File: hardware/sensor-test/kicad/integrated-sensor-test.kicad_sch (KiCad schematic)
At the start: 79 parts, among them J1 TYPE-C-31-M-12, J2 Conn_01x02, J3 USB_B_Micro, J4 Conn_02x18_Odd_Even, SW1 Conn_02x18_Odd_Even, U1 NCP1117-3.3_SOT223, U10 USBLC6-2SC6, U103 RP2040, U2 W25Q128JVS, U3 AP2112K-3.3TRG1, U4 TPS22919DCKR, U5 TMUX1208PWR, U6 DRV5055A3QDBZR, U7 DRV5055A3QDBZR, U8 DRV5055A3QDBZR, U9 DRV5055A3QDBZR, Y1 ABLS-12.000MHZ-B4-T

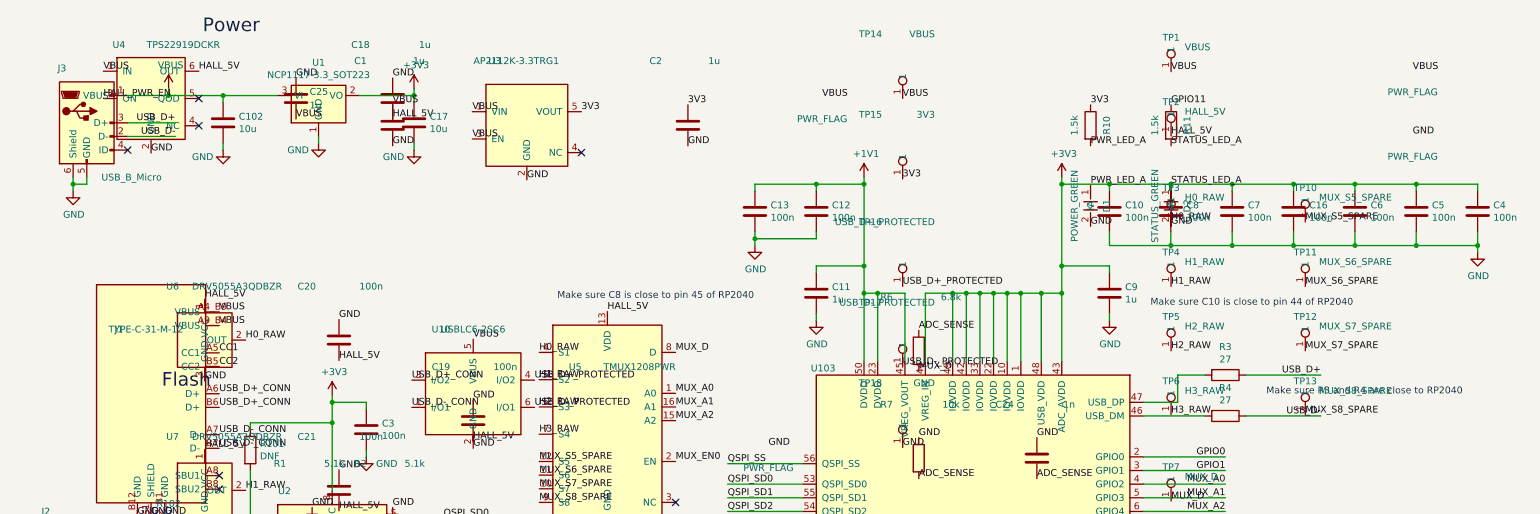
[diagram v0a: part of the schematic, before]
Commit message: Fix integrated schematic power declarations
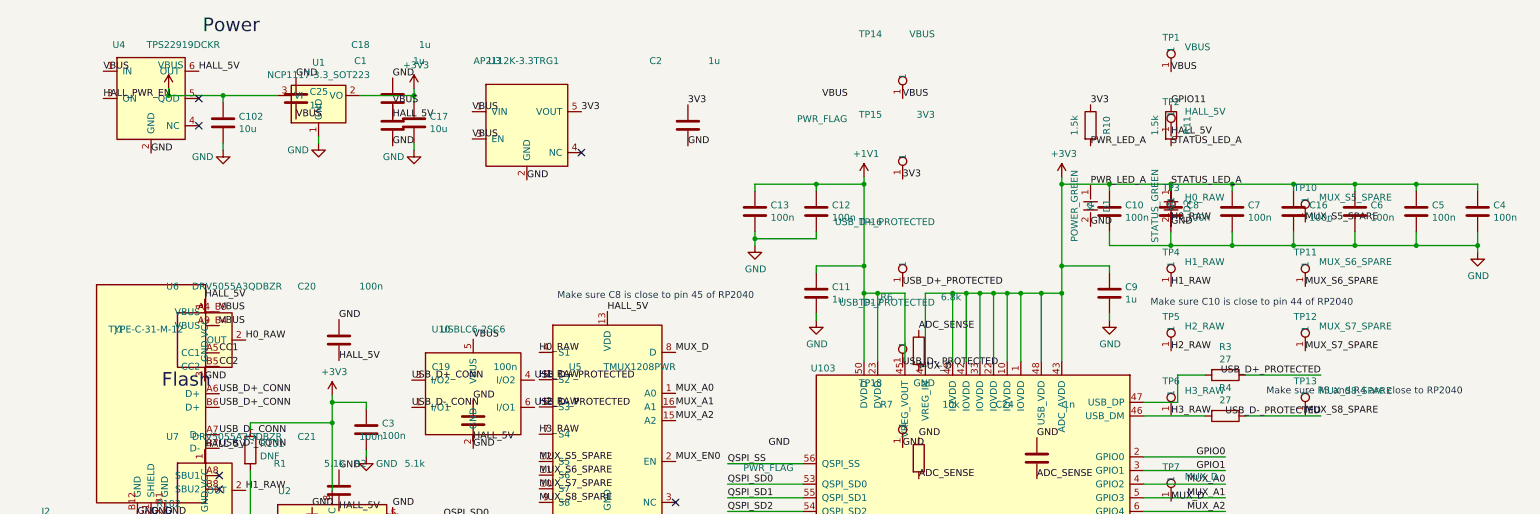
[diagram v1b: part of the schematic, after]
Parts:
- removed J3: USB_B_Micro, RP2040_minimal:USB_Micro-B_Amphenol_10103594-0001LF_Horizontal_modified, symbol RP2040_minimal-rescue:USB_B_Micro-Connector
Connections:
- net USB_D+ is gone; now on net USB_D+_PROTECTED: R3.1
- net USB_D- is gone; now on net USB_D-_PROTECTED: R4.1
- no-connect marks 7 -> 6
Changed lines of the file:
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@@
   (junction (at 312.42 142.24) (diameter 0) (color 0 0 0 0)
     )
-  (junction (at 30.48 60.96) (diameter 0) (color 0 0 0 0)
-    )
   (junction (at 214.63 81.28) (diameter 0) (color 0 0 0 0)
     )
@@
   (junction (at 48.26 44.45) (diameter 0) (color 0 0 0 0)
     )
-  (no_connect (at 40.64 54.61))
   (wire (pts (xy 196.85 93.98) (xy 196.85 81.28))
       (stroke (width 0) (type default))
@@
       (stroke (width 0) (type default))
     )
-  (wire (pts (xy 30.48 60.96) (xy 30.48 62.23))
-      (stroke (width 0) (type default))
-    )
   (wire (pts (xy 236.22 96.52) (xy 236.22 101.6))
       (stroke (width 0) (type default))
@@
       (stroke (width 0) (type default))
     )
-  (wire (pts (xy 30.48 59.69) (xy 30.48 60.96))
-      (stroke (width 0) (type default))
-    )
   (wire (pts (xy 280.67 69.85) (xy 280.67 72.39))
       (stroke (width 0) (type default))
@@
       (stroke (width 0) (type default))
     )
-  (wire (pts (xy 40.64 49.53) (xy 49.53 49.53))
-      (stroke (width 0) (type default))
-    )
   (wire (pts (xy 312.42 124.46) (xy 312.42 127))
       (stroke (width 0) (type default))
@@
       (stroke (width 0) (type default))
     )
-  (wire (pts (xy 33.02 59.69) (xy 33.02 60.96))
-      (stroke (width 0) (type default))
-    )
   (wire (pts (xy 152.4 116.84) (xy 166.37 116.84))
       (stroke (width 0) (type default))
@@
       (stroke (width 0) (type default))
     )
-  (wire (pts (xy 40.64 52.07) (xy 49.53 52.07))
-      (stroke (width 0) (type default))
-    )
   (wire (pts (xy 229.87 104.14) (xy 241.3 104.14))
       (stroke (width 0) (type default))
@@
       (stroke (width 0) (type default))
     )
-  (wire (pts (xy 40.64 44.45) (xy 48.26 44.45))
-      (stroke (width 0) (type default))
-    )
   (wire (pts (xy 339.09 144.78) (xy 326.39 144.78))
       (stroke (width 0) (type default))
@@
       (stroke (width 0) (type default))
     )
-  (wire (pts (xy 33.02 60.96) (xy 30.48 60.96))
-      (stroke (width 0) (type default))
-    )
   (wire (pts (xy 246.38 60.96) (xy 257.81 60.96))
       (stroke (width 0) (type default))
@@
       (effects (font (size 1.27 1.27)) (justify right bottom))
     )
-  (label "USB_D+" (at 262.89 96.52 180) (fields_autoplaced)
+  (label "USB_D+_PROTECTED" (at 262.89 96.52 180) (fields_autoplaced)
       (effects (font (size 1.27 1.27)) (justify right bottom))
     )
@@
       (effects (font (size 1.27 1.27)) (justify right bottom))
     )
-  (label "USB_D+" (at 49.53 49.53 180) (fields_autoplaced)
-      (effects (font (size 1.27 1.27)) (justify right bottom))
-    )
   (label "GPIO1" (at 339.09 127 180) (fields_autoplaced)
       (effects (font (size 1.27 1.27)) (justify right bottom))
@@
       (effects (font (size 1.27 1.27)) (justify right bottom))
     )
-  (label "USB_D-" (at 49.53 52.07 180) (fields_autoplaced)
-      (effects (font (size 1.27 1.27)) (justify right bottom))
-    )
   (label "GPIO20" (at 358.14 144.78 0) (fields_autoplaced)
       (effects (font (size 1.27 1.27)) (justify left bottom))
@@
       (effects (font (size 1.27 1.27)) (justify left bottom))
     )
-  (label "USB_D-" (at 262.89 104.14 180) (fields_autoplaced)
+  (label "USB_D-_PROTECTED" (at 262.89 104.14 180) (fields_autoplaced)
       (effects (font (size 1.27 1.27)) (justify right bottom))
     )
@@
       )
     )
-  (symbol (lib_id "RP2040_minimal-rescue:USB_B_Micro-Connector") (at 33.02 49.53 0) (unit 1)
-      (in_bom yes) (on_board yes) (dnp no)
-      (property "Reference" "J3" (at 29.21 39.37 0)
-        (effects (font (size 1.27 1.27)) (justify right))
-      )
-      (property "Value" "USB_B_Micro" (at 46.99 59.69 0)
-        (effects (font (size 1.27 1.27)) (justify right))
-      )
-      (property "Footprint" "RP2040_minimal:USB_Micro-B_Amphenol_10103594-0001LF_Horizontal_modified" (at 36.83 50.8 0)
-        (effects (font (size 1.27 1.27)) hide)
-      )
-      (property "Datasheet" "https://datasheet.lcsc.com/lcsc/1912111437_Amphenol-ICC-10103594-0001LF_C428495.pdf" (at 36.83 50.8 0)
-        (effects (font (size 1.27 1.27)) hide)
-      )
-      (property "LCSC" "C428495" (at 33.02 49.53 0)
-        (effects (font (size 1.27 1.27)) hide)
-      )
-      (pin "1")
-      (pin "2")
-      (pin "3")
-      (pin "4")
-      (pin "5")
-      (pin "6")
-      (instances
-        (project "he-piantor-sensor-test"
-          (path "/0b572f4d-42c2-4e67-a259-3bf815f1855a"
-            (reference "J3") (unit 1)
-          )
-        )
-      )
-    )
   (symbol (lib_id "power:GND") (at 198.12 198.12 0) (unit 1)
       (in_bom yes) (on_board yes) (dnp no)
@@
       )
     )
-  (symbol (lib_id "power:GND") (at 30.48 62.23 0) (unit 1)
-      (in_bom yes) (on_board yes) (dnp no)
-      (property "Reference" "#PWR01" (at 30.48 68.58 0)
-        (effects (font (size 1.27 1.27)) hide)
-      )
-      (property "Value" "GND" (at 30.607 66.6242 0)
-        (effects (font (size 1.27 1.27)))
-      )
-      (property "Footprint" "" (at 30.48 62.23 0)
-        (effects (font (size 1.27 1.27)) hide)
-      )
-      (property "Datasheet" "" (at 30.48 62.23 0)
-        (effects (font (size 1.27 1.27)) hide)
-      )
-      (pin "1")
-      (instances
-        (project "he-piantor-sensor-test"
-          (path "/0b572f4d-42c2-4e67-a259-3bf815f1855a"
-            (reference "#PWR01") (unit 1)
-          )
-        )
-      )
-    )
   (symbol (lib_id "power:GND") (at 339.09 166.37 0) (mirror y) (unit 1)
       (in_bom yes) (on_board yes) (dnp no)
@@
       (effects (font (size 1.27 1.27)) (justify left bottom))
     )
-  (symbol (lib_id "power:PWR_FLAG") (at 280 40 0) (unit 1)
-      (in_bom yes) (on_board yes) (dnp no)
-      (property "Reference" "#FLG03" (at 280 41.905 0) (effects (font (size 1.27 1.27)) hide))
-      (property "Value" "PWR_FLAG" (at 280 43.81 0) (effects (font (size 1.27 1.27))))
-      (property "Footprint" "" (at 280 40 0) (effects (font (size 1.27 1.27)) hide))
-      (property "Datasheet" "~" (at 280 40 0) (effects (font (size 1.27 1.27)) hide))
-      (pin "1")
-      (instances (project "hall-front-end" (path "/a1000000-0000-0000-0000-000000000001" (reference "#FLG03") (unit 1))))
-    )
-  (label "VBUS" (at 280 40 0) (effects (font (size 1.27 1.27)) (justify left bottom)))
-  (symbol (lib_id "power:PWR_FLAG") (at 280 52 0) (unit 1)
-      (in_bom yes) (on_board yes) (dnp no)
-      (property "Reference" "#FLG04" (at 280 53.905 0) (effects (font (size 1.27 1.27)) hide))
-      (property "Value" "PWR_FLAG" (at 280 55.81 0) (effects (font (size 1.27 1.27))))
-      (property "Footprint" "" (at 280 52 0) (effects (font (size 1.27 1.27)) hide))
-      (property "Datasheet" "~" (at 280 52 0) (effects (font (size 1.27 1.27)) hide))
-      (pin "1")
-      (instances (project "hall-front-end" (path "/a1000000-0000-0000-0000-000000000001" (reference "#FLG04") (unit 1))))
-    )
-  (label "GND" (at 280 52 0) (effects (font (size 1.27 1.27)) (justify left bottom)))
   (symbol (lib_id "Device:R") (at 235 50 0) (unit 1)
     (in_bom yes) (on_board yes) (dnp no)

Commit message: Remove RP2040 reference-only circuitry
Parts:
- removed C102: 10u, Capacitor_SMD:C_0805_2012Metric, symbol Device:C
- removed J4, SW1: Conn_02x18_Odd_Even, Connector_PinHeader_2.54mm:PinHeader_2x18_P2.54mm_Vertical, symbol Connector_Generic:Conn_02x18_Odd_Even
- removed U1: NCP1117-3.3_SOT223, Package_TO_SOT_SMD:SOT-223-3_TabPin2, symbol Regulator_Linear:NCP1117-3.3_SOT223
- added TP19: SWDIO, TestPoint:TestPoint_Pad_D1.5mm, symbol Connector:TestPoint
- added TP20: SWCLK, TestPoint:TestPoint_Pad_D1.5mm, symbol Connector:TestPoint
- added TP21: RUN, TestPoint:TestPoint_Pad_D1.5mm, symbol Connector:TestPoint
- C14, C15: value 27p -> 15p; LCSC C52923 -> (none)
- R5: footprint Capacitor_SMD:C_0402_1005Metric -> Resistor_SMD:R_0402_1005Metric
- TP15: value 3V3 -> +3V3
- U2: value W25Q128JVS -> W25Q16JVUXIQ; footprint Package_SO:SOIC-8_5.23x5.23mm_P1.27mm -> Package_DFN_QFN:USON-8-1EP_2x3mm_P0.5mm_EP0.61x2.2mm; symbol RP2040_minimal-rescue:W25Q128JVS-Memory_Flash -> HEP:W25Q16JVUXIQ; LCSC C97521 -> C2843335
- Y1: value ABLS-12.000MHZ-B4-T -> ABM8-272-T3; footprint RP2040_minimal:Crystal_SMD_HC49-US -> Crystal:Crystal_SMD_Abracon_ABM8G-2Pin_3.2x2.5mm; LCSC C110563 -> C20625731
- renumbered U103 to U1
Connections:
- net 3V3 is gone; now on net +3V3: C2.1, R10.1, TP15.1, U3.5 (VOUT)
- net RUN: now also TP21.1
- net SWCLK: now also TP20.1
- net SWD: now also TP19.1

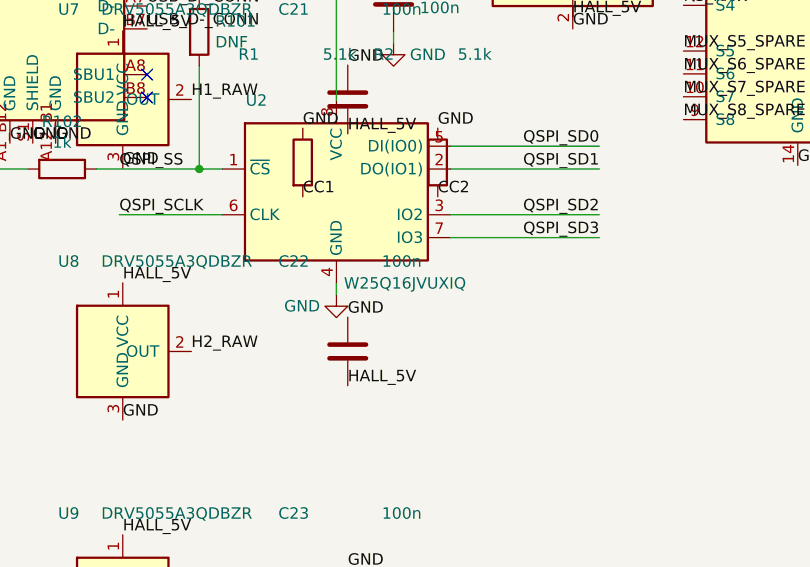
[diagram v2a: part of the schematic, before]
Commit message: Restore loadable flash symbol definition
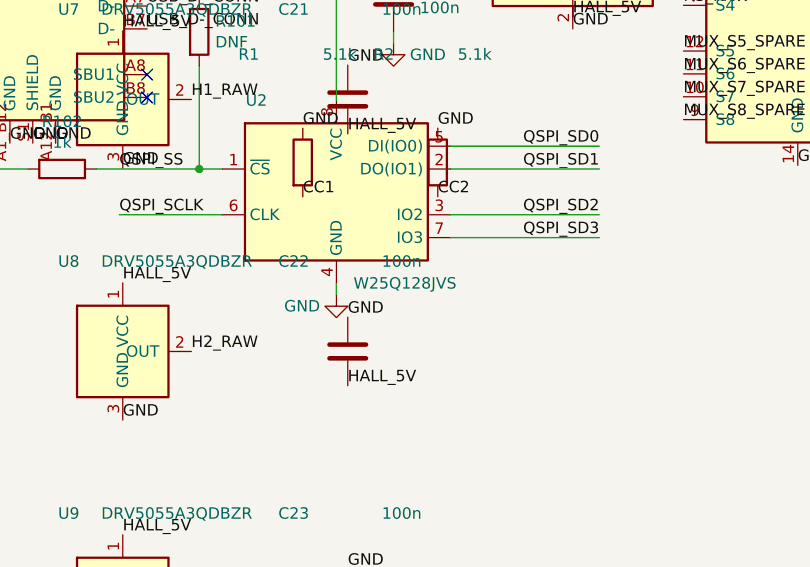
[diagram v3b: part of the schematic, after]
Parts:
- U2: value W25Q16JVUXIQ -> W25Q128JVS; footprint Package_DFN_QFN:USON-8-1EP_2x3mm_P0.5mm_EP0.61x2.2mm -> Package_SO:SOIC-8_5.23x5.23mm_P1.27mm; symbol HEP:W25Q16JVUXIQ -> RP2040_minimal-rescue:W25Q128JVS-Memory_Flash; LCSC C2843335 -> C97521
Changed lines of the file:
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@@
       )
     )
-  (symbol (lib_id "HEP:W25Q16JVUXIQ") (at 78.74 128.27 0) (unit 1)
+  (symbol (lib_id "RP2040_minimal-rescue:W25Q128JVS-Memory_Flash") (at 78.74 128.27 0) (unit 1)
       (in_bom yes) (on_board yes) (dnp no)
       (property "Reference" "U2" (at 69.85 118.11 0)
         (effects (font (size 1.27 1.27)))
       )
-      (property "Value" "W25Q16JVUXIQ" (at 86.36 138.43 0)
+      (property "Value" "W25Q128JVS" (at 86.36 138.43 0)
         (effects (font (size 1.27 1.27)))
       )
-      (property "Footprint" "Package_DFN_QFN:USON-8-1EP_2x3mm_P0.5mm_EP0.61x2.2mm" (at 78.74 128.27 0)
+      (property "Footprint" "Package_SO:SOIC-8_5.23x5.23mm_P1.27mm" (at 78.74 128.27 0)
         (effects (font (size 1.27 1.27)) hide)
       )
-      (property "Datasheet" "https://www.winbond.com/resource-files/w25q16jv%20spi%20revg%2003222018%20plus.pdf" (at 78.74 128.27 0)
+      (property "Datasheet" "http://www.winbond.com/resource-files/w25q128jv_dtr%20revc%2003272018%20plus.pdf" (at 78.74 128.27 0)
         (effects (font (size 1.27 1.27)) hide)
       )
-      (property "LCSC" "C2843335" (at 78.74 128.27 0)
+      (property "LCSC" "C97521" (at 78.74 128.27 0)
         (effects (font (size 1.27 1.27)) hide)
       )
